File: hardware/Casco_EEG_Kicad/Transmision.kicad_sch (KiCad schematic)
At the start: 5 parts, among them SW1 SW_Push, U1 HC-05

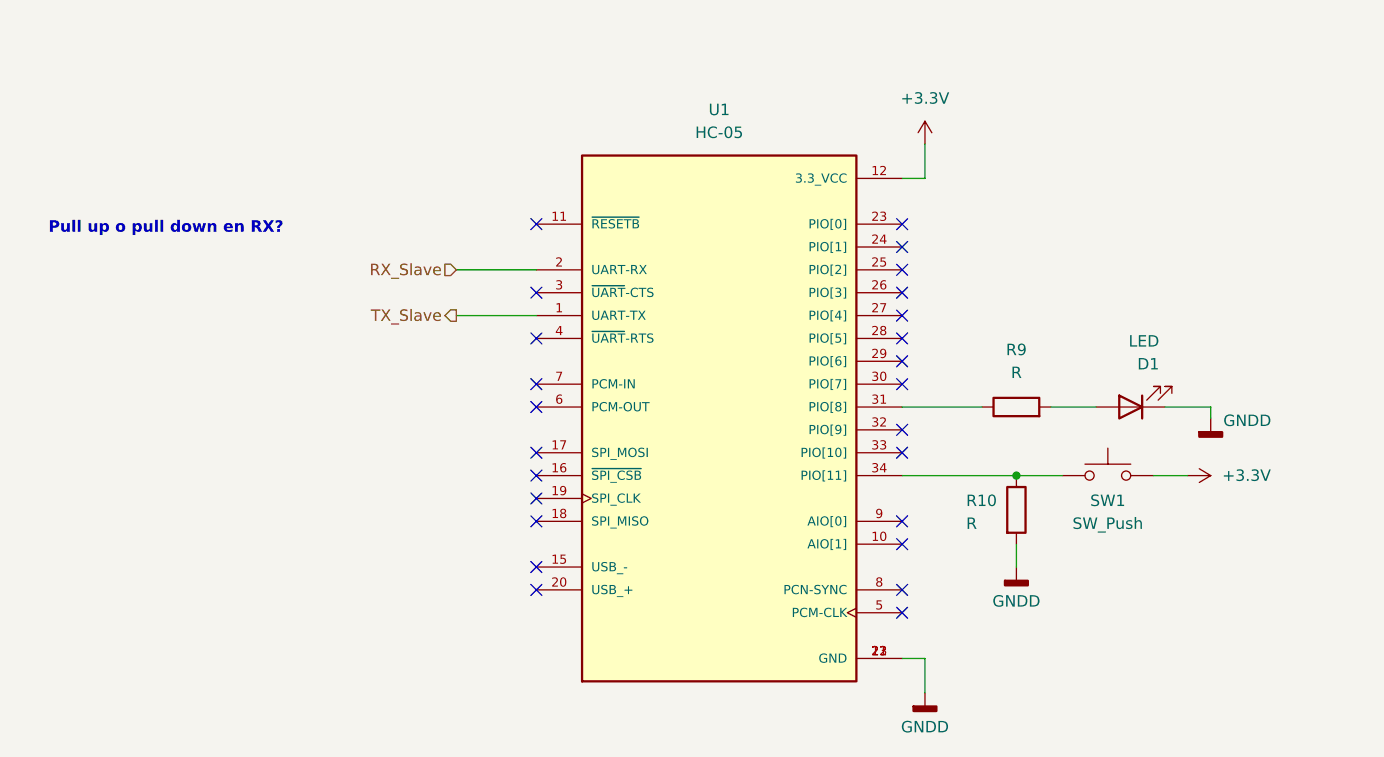
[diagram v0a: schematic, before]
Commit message: Primera implementacion de PCB, cambios varios
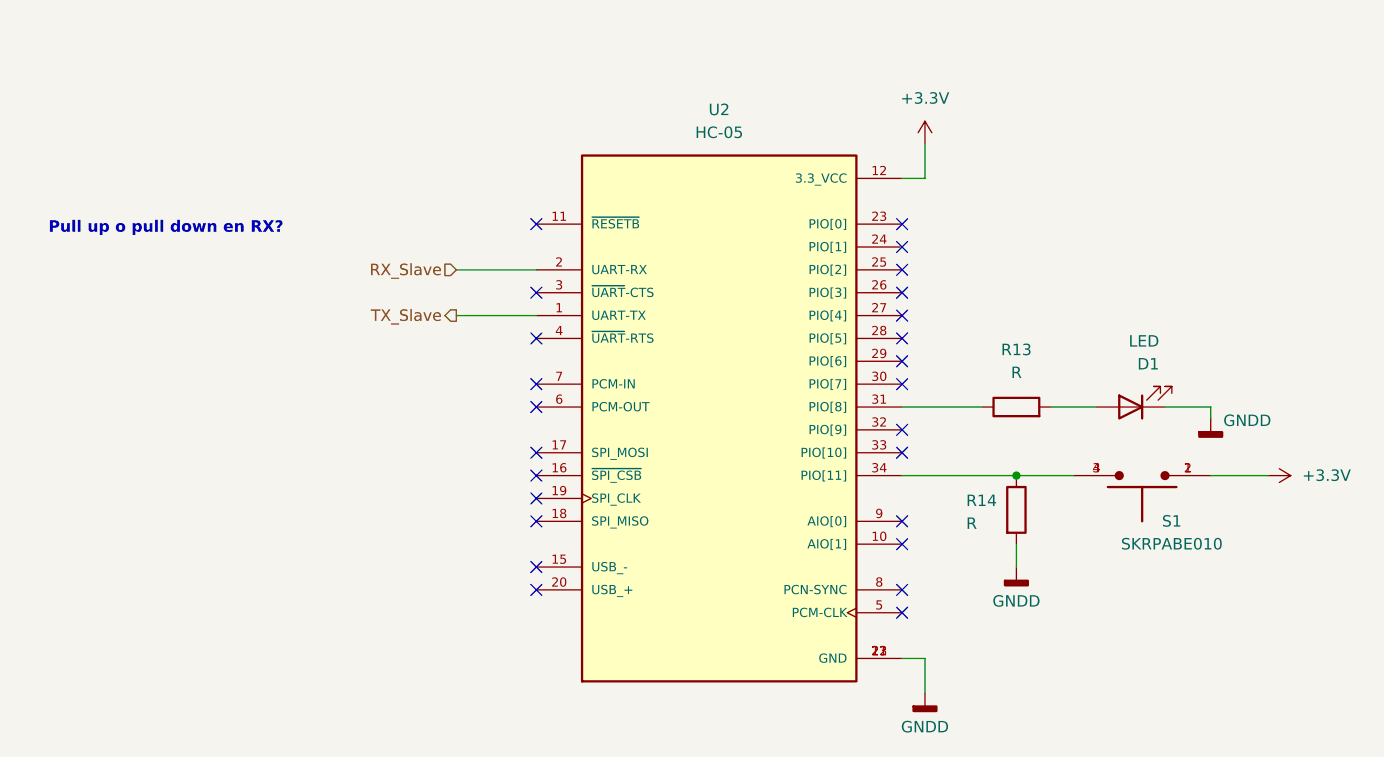
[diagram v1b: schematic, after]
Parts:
- removed SW1: SW_Push, symbol Switch:SW_Push
- added S1: SKRPABE010, Huellas:SW_SKRPABE010, symbol SWButton:SKRPABE010
- D1: footprint (none) -> LED_SMD:LED_0603_1608Metric
- R13: renamed from R9; footprint (none) -> Resistor_SMD:R_0603_1608Metric
- R14: renamed from R10; footprint (none) -> Resistor_SMD:R_0603_1608Metric
- renumbered U1 to U2
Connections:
- net +3.3V: now also S1.1, S1.2
- net at R14.1, U2.34 (PIO[11]): now also S1.3, S1.4

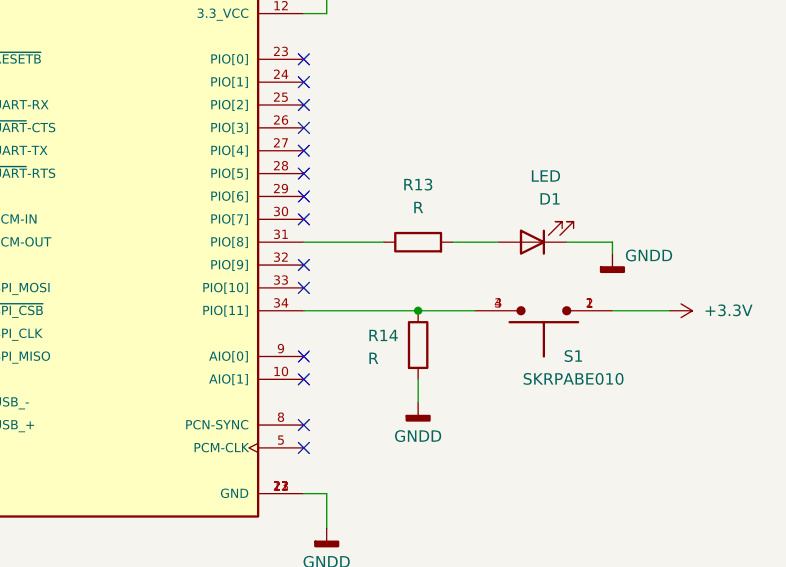
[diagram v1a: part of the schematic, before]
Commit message: Nuevos cambios al PCB, mejoro planos, regulo 3,3V desde 5V, etc
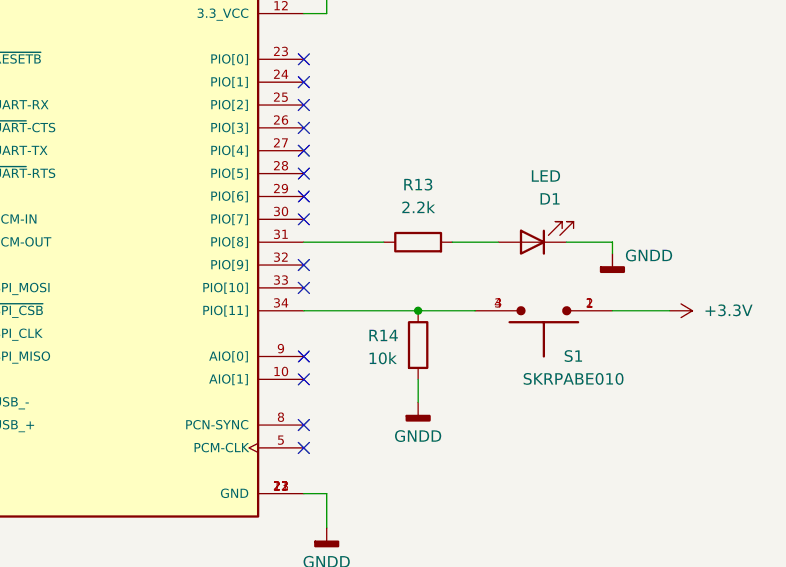
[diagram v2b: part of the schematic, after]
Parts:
- D1: LCSC PN (none) -> C19171394
- R13: value R -> 2.2k
- R14: value R -> 10k; LCSC PN (none) -> C25804
- S1: LCSC PN (none) -> C115360
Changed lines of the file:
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@@
+			)
+		)
+		(property "LCSC PN" "C19171394"
+			(at 180.34 83.82 0)
+			(effects
+				(font
+					(size 1.27 1.27)
+				)
+				(hide yes)
 			)
 		)
@@
 			)
 		)
-		(property "Value" "R"
+		(property "Value" "2.2k"
 			(at 167.64 80.01 90)
 			(effects
@@
 			)
 		)
-		(property "Value" "R"
+		(property "Value" "10k"
 			(at 162.052 96.774 0)
 			(effects
@@
 		)
 		(property "Description" "Resistor"
+			(at 167.64 95.25 0)
+			(effects
+				(font
+					(size 1.27 1.27)
+				)
+				(hide yes)
+			)
+		)
+		(property "LCSC PN" "C25804"
 			(at 167.64 95.25 0)
 			(effects
@@
 				(hide yes)
 			)
+		)
+		(property "LCSC PN" "C115360"
+			(at 181.61 91.44 0)
+			(effects
+				(font
+					(size 1.27 1.27)
+				)
+				(hide yes)
+			)

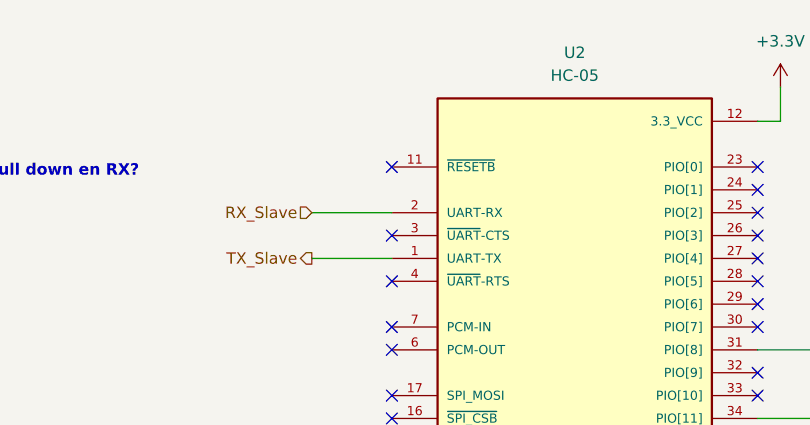
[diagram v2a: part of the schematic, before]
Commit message: Implemento pines I/O para trigger
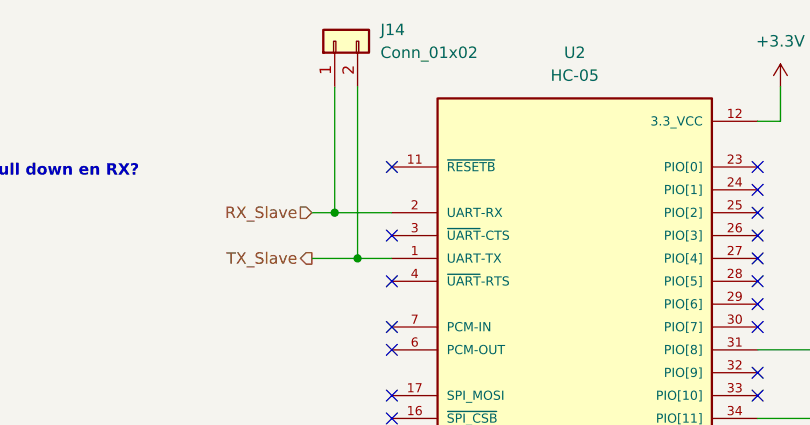
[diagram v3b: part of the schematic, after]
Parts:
- added J14: Conn_01x02, Connector_PinHeader_2.54mm:PinHeader_1x02_P2.54mm_Vertical, symbol Connector_Generic:Conn_01x02
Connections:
- net RX_Slave: now also J14.1 (Pin_1)
- net TX_Slave: now also J14.2 (Pin_2)
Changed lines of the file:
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@@
+	)
+	(junction
+		(at 107.95 68.58)
+		(diameter 0)
+		(color 0 0 0 0)
 	)
 	(junction
@@
 		(color 0 0 0 0)
 	)
+	(junction
+		(at 110.49 73.66)
+		(diameter 0)
+		(color 0 0 0 0)
+	)
 	(no_connect
 		(at 114.3 76.2)
@@
 	(wire
 		(pts
-			(xy 105.41 68.58) (xy 114.3 68.58)
+			(xy 105.41 68.58) (xy 107.95 68.58)
 		)
 		(stroke
@@
 	(wire
 		(pts
-			(xy 167.64 99.06) (xy 167.64 101.6)
+			(xy 107.95 54.61) (xy 107.95 68.58)
 		)
 		(stroke
@@
 	(wire
 		(pts
-			(xy 157.48 58.42) (xy 154.94 58.42)
+			(xy 167.64 99.06) (xy 167.64 101.6)
 		)
 		(stroke
@@
 	(wire
 		(pts
-			(xy 154.94 111.76) (xy 157.48 111.76)
+			(xy 157.48 58.42) (xy 154.94 58.42)
 		)
 		(stroke
@@
 	(wire
 		(pts
-			(xy 157.48 111.76) (xy 157.48 115.57)
+			(xy 154.94 111.76) (xy 157.48 111.76)
 		)
 		(stroke
@@
 	(wire
 		(pts
-			(xy 189.23 91.44) (xy 195.58 91.44)
+			(xy 157.48 111.76) (xy 157.48 115.57)
 		)
 		(stroke
@@
 	(wire
 		(pts
-			(xy 167.64 91.44) (xy 173.99 91.44)
+			(xy 189.23 91.44) (xy 195.58 91.44)
 		)
 		(stroke
@@
 	(wire
 		(pts
-			(xy 105.41 73.66) (xy 114.3 73.66)
+			(xy 167.64 91.44) (xy 173.99 91.44)
+		)
+		(stroke
+			(width 0)
+			(type default)
+		)
+	)
+	(wire
+		(pts
+			(xy 110.49 73.66) (xy 114.3 73.66)
+		)
+		(stroke
+			(width 0)
+			(type default)
+		)
+	)
+	(wire
+		(pts
+			(xy 107.95 68.58) (xy 114.3 68.58)
+		)
+		(stroke
+			(width 0)
+			(type default)
+		)
+	)
+	(wire
+		(pts
+			(xy 105.41 73.66) (xy 110.49 73.66)
+		)
+		(stroke
+			(width 0)
+			(type default)
+		)
+	)
+	(wire
+		(pts
+			(xy 110.49 54.61) (xy 110.49 73.66)
 		)
 		(stroke
@@
 					(unit 1)
 				)
+			)
+		)
+	)
+	(symbol
+		(lib_id "Connector_Generic:Conn_01x02")
+		(at 107.95 49.53 90)
+		(unit 1)
+		(exclude_from_sim no)
+		(in_bom yes)
+		(on_board yes)
+		(dnp no)
+		(fields_autoplaced yes)
+		(property "Reference" "J14"
+			(at 113.03 48.2599 90)
+			(effects
+				(font
+					(size 1.27 1.27)
+				)
+				(justify right)
+			)
+		)
+		(property "Value" "Conn_01x02"
+			(at 113.03 50.7999 90)
+			(effects
+				(font
+					(size 1.27 1.27)
+				)
+				(justify right)
+			)
+		)
+		(property "Footprint" "Connector_PinHeader_2.54mm:PinHeader_1x02_P2.54mm_Vertical"
+			(at 107.95 49.53 0)
+			(effects
+				(font
+					(size 1.27 1.27)
+				)
+				(hide yes)
+			)
+		)
+		(property "Datasheet" "~"
+			(at 107.95 49.53 0)
+			(effects
+				(font
+					(size 1.27 1.27)
+				)
+				(hide yes)
+			)
+		)
+		(property "Description" "Generic connector, single row, 01x02, script generated (kicad-library-utils/schlib/autogen/connector/)"
+			(at 107.95 49.53 0)
+			(effects
+				(font
+					(size 1.27 1.27)
+				)
+				(hide yes)
+			)
+		)
+		(pin "2"
+		)
+		(pin "1"
+		)
+		(instances
+			(project ""
+				(path "/3414db36-80da-469c-8b48-81d6bd2f8966/fe171ca0-0165-4621-a7c1-0aa23dfd8c22"
+					(reference "J14")
+					(unit 1)
+				)

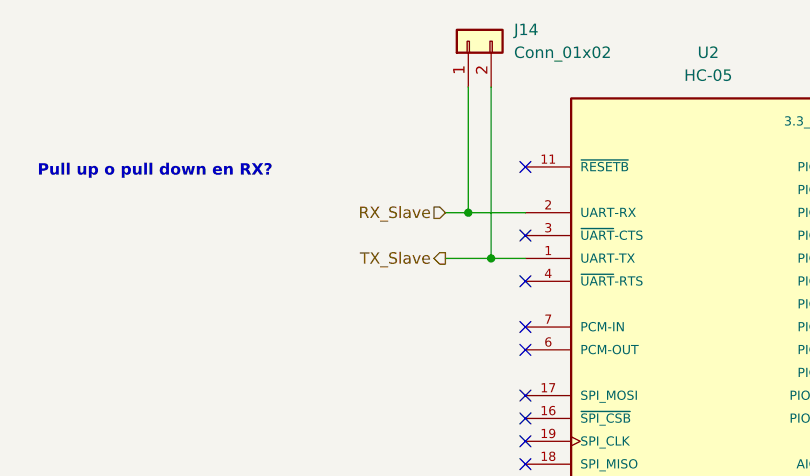
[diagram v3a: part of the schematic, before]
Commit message: Actualizacion del modelo, agrego mini slide switch, agrego jumpers para comunicacion con modulo BT
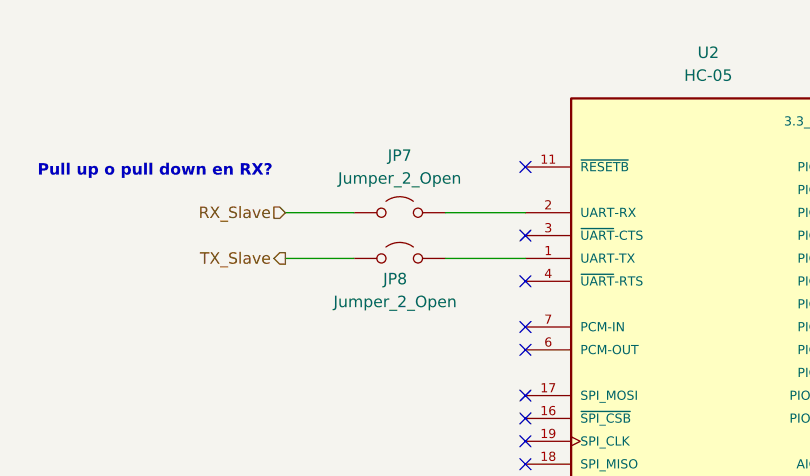
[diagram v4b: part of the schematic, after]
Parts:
- removed J14: Conn_01x02, Connector_PinHeader_2.54mm:PinHeader_1x02_P2.54mm_Vertical, symbol Connector_Generic:Conn_01x02
- added JP7, JP8: Jumper_2_Open, Connector_PinHeader_2.54mm:PinHeader_1x02_P2.54mm_Vertical, symbol Jumper:Jumper_2_Open
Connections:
- net RX_Slave: now also JP7.1 (A); no longer U2.2 (UART-RX)
- net TX_Slave: now also JP8.1 (A); no longer U2.1 (UART-TX)
- new net: JP8.2 (B), U2.1 (UART-TX)
- new net: JP7.2 (B), U2.2 (UART-RX)
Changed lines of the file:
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@@
 	)
 	(junction
-		(at 107.95 68.58)
-		(diameter 0)
-		(color 0 0 0 0)
-	)
-	(junction
 		(at 167.64 91.44)
 		(diameter 0)
 		(color 0 0 0 0)
 	)
-	(junction
-		(at 110.49 73.66)
-		(diameter 0)
-		(color 0 0 0 0)
-	)
 	(no_connect
 		(at 114.3 76.2)
@@
 	(wire
 		(pts
-			(xy 105.41 68.58) (xy 107.95 68.58)
+			(xy 157.48 54.61) (xy 157.48 58.42)
 		)
 		(stroke
@@
 	(wire
 		(pts
-			(xy 157.48 54.61) (xy 157.48 58.42)
+			(xy 105.41 68.58) (xy 114.3 68.58)
 		)
 		(stroke
@@
 	(wire
 		(pts
-			(xy 189.23 83.82) (xy 189.23 85.09)
+			(xy 87.63 68.58) (xy 95.25 68.58)
 		)
 		(stroke
@@
 	(wire
 		(pts
-			(xy 107.95 54.61) (xy 107.95 68.58)
+			(xy 189.23 83.82) (xy 189.23 85.09)
 		)
 		(stroke
@@
 	(wire
 		(pts
-			(xy 154.94 111.76) (xy 157.48 111.76)
-		)
-		(stroke
-			(width 0)
-			(type default)
-		)
-	)
-	(wire
-		(pts
-			(xy 157.48 111.76) (xy 157.48 115.57)
-		)
-		(stroke
-			(width 0)
-			(type default)
-		)
-	)
-	(wire
-		(pts
-			(xy 189.23 91.44) (xy 195.58 91.44)
+			(xy 87.63 73.66) (xy 95.25 73.66)
 		)
 		(stroke
@@
 	(wire
 		(pts
-			(xy 167.64 91.44) (xy 173.99 91.44)
+			(xy 154.94 111.76) (xy 157.48 111.76)
 		)
 		(stroke
@@
 	(wire
 		(pts
-			(xy 110.49 73.66) (xy 114.3 73.66)
+			(xy 105.41 73.66) (xy 114.3 73.66)
 		)
 		(stroke
@@
 	(wire
 		(pts
-			(xy 107.95 68.58) (xy 114.3 68.58)
+			(xy 157.48 111.76) (xy 157.48 115.57)
 		)
 		(stroke
@@
 	(wire
 		(pts
-			(xy 105.41 73.66) (xy 110.49 73.66)
+			(xy 189.23 91.44) (xy 195.58 91.44)
 		)
 		(stroke
@@
 	(wire
 		(pts
-			(xy 110.49 54.61) (xy 110.49 73.66)
+			(xy 167.64 91.44) (xy 173.99 91.44)
 		)
 		(stroke
@@
 	(hierarchical_label "TX_Slave"
 		(shape output)
-		(at 105.41 73.66 180)
+		(at 87.63 73.66 180)
 		(effects
 			(font
@@
 	(hierarchical_label "RX_Slave"
 		(shape input)
-		(at 105.41 68.58 180)
+		(at 87.63 68.58 180)
 		(effects
 			(font
@@
 	)
 	(symbol
-		(lib_id "Connector_Generic:Conn_01x02")
-		(at 107.95 49.53 90)
-		(unit 1)
-		(exclude_from_sim no)
-		(in_bom yes)
-		(on_board yes)
-		(dnp no)
-		(fields_autoplaced yes)
-		(property "Reference" "J14"
-			(at 113.03 48.2599 90)
-			(effects
-				(font
-					(size 1.27 1.27)
-				)
-				(justify right)
-			)
-		)
-		(property "Value" "Conn_01x02"
-			(at 113.03 50.7999 90)
-			(effects
-				(font
-					(size 1.27 1.27)
-				)
-				(justify right)
-			)
-		)
-		(property "Footprint" "Connector_PinHeader_2.54mm:PinHeader_1x02_P2.54mm_Vertical"
-			(at 107.95 49.53 0)
-			(effects
-				(font
-					(size 1.27 1.27)
-				)
-				(hide yes)
-			)
-		)
-		(property "Datasheet" "~"
-			(at 107.95 49.53 0)
-			(effects
-				(font
-					(size 1.27 1.27)
-				)
-				(hide yes)
-			)
-		)
-		(property "Description" "Generic connector, single row, 01x02, script generated (kicad-library-utils/schlib/autogen/connector/)"
-			(at 107.95 49.53 0)
-			(effects
-				(font
-					(size 1.27 1.27)
-				)
-				(hide yes)
-			)
-		)
-		(pin "2"
-		)
-		(pin "1"
-		)
-		(instances
-			(project ""
-				(path "/3414db36-80da-469c-8b48-81d6bd2f8966/fe171ca0-0165-4621-a7c1-0aa23dfd8c22"
-					(reference "J14")
-					(unit 1)
-				)
-			)
-		)
-	)
-	(symbol
 		(lib_id "Device:R")
 		(at 167.64 83.82 90)
@@
 	)
 	(symbol
+		(lib_id "Jumper:Jumper_2_Open")
+		(at 100.33 73.66 0)
+		(unit 1)
+		(exclude_from_sim no)
+		(in_bom yes)
+		(on_board yes)
+		(dnp no)
+		(property "Reference" "JP8"
+			(at 99.822 75.946 0)
+			(effects
+				(font
+					(size 1.27 1.27)
+				)
+			)
+		)
+		(property "Value" "Jumper_2_Open"
+			(at 99.822 78.486 0)
+			(effects
+				(font
+					(size 1.27 1.27)
+				)
+			)
+		)
+		(property "Footprint" "Connector_PinHeader_2.54mm:PinHeader_1x02_P2.54mm_Vertical"
+			(at 100.33 73.66 0)
+			(effects
+				(font
+					(size 1.27 1.27)
+				)
+				(hide yes)
+			)
+		)
+		(property "Datasheet" "~"
+			(at 100.33 73.66 0)
+			(effects
+				(font
+					(size 1.27 1.27)
+				)
+				(hide yes)
+			)
+		)
+		(property "Description" "Jumper, 2-pole, open"
+			(at 100.33 73.66 0)
+			(effects
+				(font
+					(size 1.27 1.27)
+				)
+				(hide yes)
+			)
+		)
+		(pin "1"
+		)
+		(pin "2"
+		)
+		(instances
+			(project "Casco_EEG_Kicad"
+				(path "/3414db36-80da-469c-8b48-81d6bd2f8966/fe171ca0-0165-4621-a7c1-0aa23dfd8c22"
+					(reference "JP8")
+					(unit 1)
+				)
+			)
+		)
+	)
+	(symbol
 		(lib_id "power:GNDD")
 		(at 189.23 85.09 0)
@@
 					(unit 1)
 				)
+			)
+		)
+	)
+	(symbol
+		(lib_id "Jumper:Jumper_2_Open")
+		(at 100.33 68.58 0)
+		(unit 1)
+		(exclude_from_sim no)
+		(in_bom yes)
+		(on_board yes)
+		(dnp no)
+		(fields_autoplaced yes)
+		(property "Reference" "JP7"
+			(at 100.33 62.23 0)
+			(effects
+				(font
+					(size 1.27 1.27)
+				)
+			)
+		)
+		(property "Value" "Jumper_2_Open"
+			(at 100.33 64.77 0)
+			(effects
+				(font
+					(size 1.27 1.27)
+				)
+			)
+		)
+		(property "Footprint" "Connector_PinHeader_2.54mm:PinHeader_1x02_P2.54mm_Vertical"
+			(at 100.33 68.58 0)
+			(effects
+				(font
+					(size 1.27 1.27)
+				)
+				(hide yes)
+			)
+		)
+		(property "Datasheet" "~"
+			(at 100.33 68.58 0)
+			(effects
+				(font
+					(size 1.27 1.27)
+				)
+				(hide yes)
+			)
+		)
+		(property "Description" "Jumper, 2-pole, open"
+			(at 100.33 68.58 0)
+			(effects
+				(font
+					(size 1.27 1.27)
+				)
+				(hide yes)
+			)
+		)
+		(pin "1"
+		)
+		(pin "2"
+		)
+		(instances
+			(project "Casco_EEG_Kicad"
+				(path "/3414db36-80da-469c-8b48-81d6bd2f8966/fe171ca0-0165-4621-a7c1-0aa23dfd8c22"
+					(reference "JP7")
+					(unit 1)
+				)

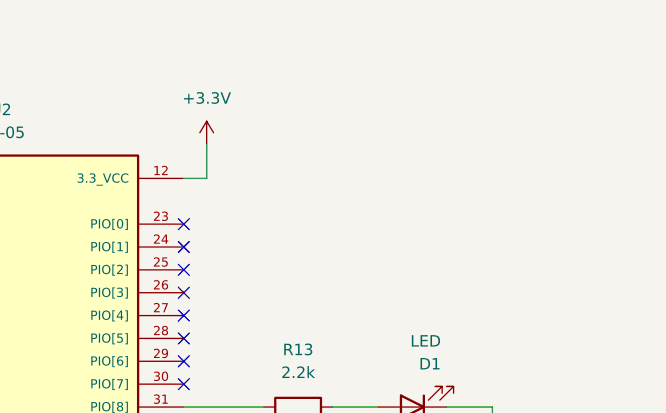
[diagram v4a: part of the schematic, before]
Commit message: Agrego protecciones a las entradas analogicas, quito jumpers dealimentacion, agrego capacitores al HC05
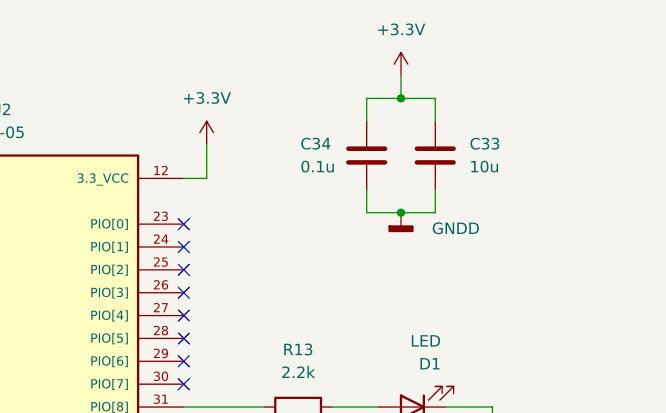
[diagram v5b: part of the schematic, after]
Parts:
- added C33: 10u, Capacitor_SMD:C_0603_1608Metric, symbol Device:C
- added C34: 0.1u, Capacitor_SMD:C_0603_1608Metric, symbol Device:C
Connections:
- net +3.3V: now also C33.1, C34.1
- net GNDD: now also C33.2, C34.2

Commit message: Cambio jumpers
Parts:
- C33: LCSC PN (none) -> C19702
- C34: LCSC PN (none) -> C14663
- R13: LCSC PN (none) -> C4190
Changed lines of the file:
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@@
+			)
+		)
+		(property "LCSC PN" "C14663"
+			(at 175.26 55.88 0)
+			(effects
+				(font
+					(size 1.27 1.27)
+				)
+				(hide yes)
 			)
 		)
@@
 			)
 		)
+		(property "LCSC PN" "C4190"
+			(at 167.64 83.82 90)
+			(effects
+				(font
+					(size 1.27 1.27)
+				)
+				(hide yes)
+			)
+		)
 		(pin "2"
 		)
@@
 			(at 182.88 55.88 0)
 			(effects
+				(font
+					(size 1.27 1.27)
+				)
+				(hide yes)
+			)
+		)
+		(property "LCSC PN" "C19702"
+			(at 182.88 55.88 0)
+			(effects
